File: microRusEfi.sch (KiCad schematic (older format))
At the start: 13 parts, among them U3 Molex_48_pin

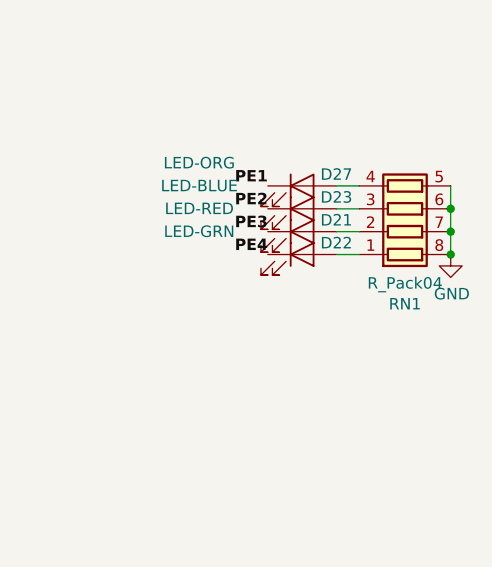
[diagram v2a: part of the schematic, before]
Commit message: Several U# were changed to RN# as they are resistor networks, not semiconductor chips. RN1 is now clearly a 1k. Also some U# were changed to CN#. BOM is now completely populated.
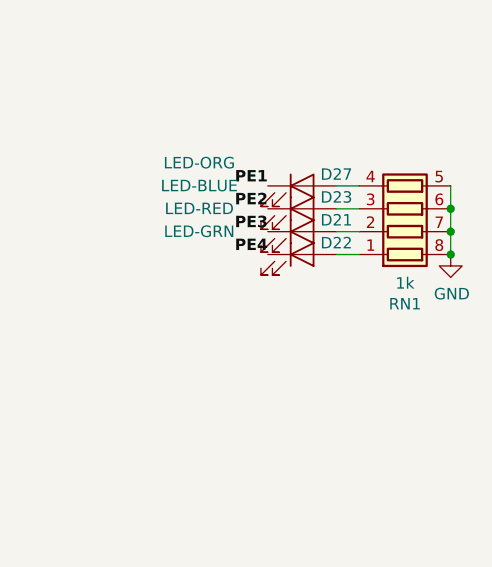
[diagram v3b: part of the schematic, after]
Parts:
- RN1: value R_Pack04 -> 1k; Manufacturer mm -> Panasonic; Part # dd -> EXB-V8V102JV; VEND# vv -> Y4102CT-ND
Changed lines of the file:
@@
 P 15000 5950
 F 0 "RN1" V 14583 5950 50  0000 C CNN
-F 1 "R_Pack04" V 14674 5950 50  0000 C CNN
+F 1 "1k" V 14674 5950 50  0000 C CNN
 F 2 "Resistor_SMD:R_Array_Convex_4x0603" V 15275 5950 50  0001 C CNN
 F 3 "~" H 15000 5950 50  0001 C CNN
-F 4 "dd" H 0   0   50  0001 C CNN "Part #"
+F 4 "EXB-V8V102JV" H 0   0   50  0001 C CNN "Part #"
 F 5 "DIGI" H 0   0   50  0001 C CNN "VEND"
-F 6 "vv" H 0   0   50  0001 C CNN "VEND#"
-F 7 "mm" H 0   0   50  0001 C CNN "Manufacturer"
+F 6 "Y4102CT-ND" H 0   0   50  0001 C CNN "VEND#"
+F 7 "Panasonic " H 0   0   50  0001 C CNN "Manufacturer"
 	1    15000 5950
 	0    1    -1   0

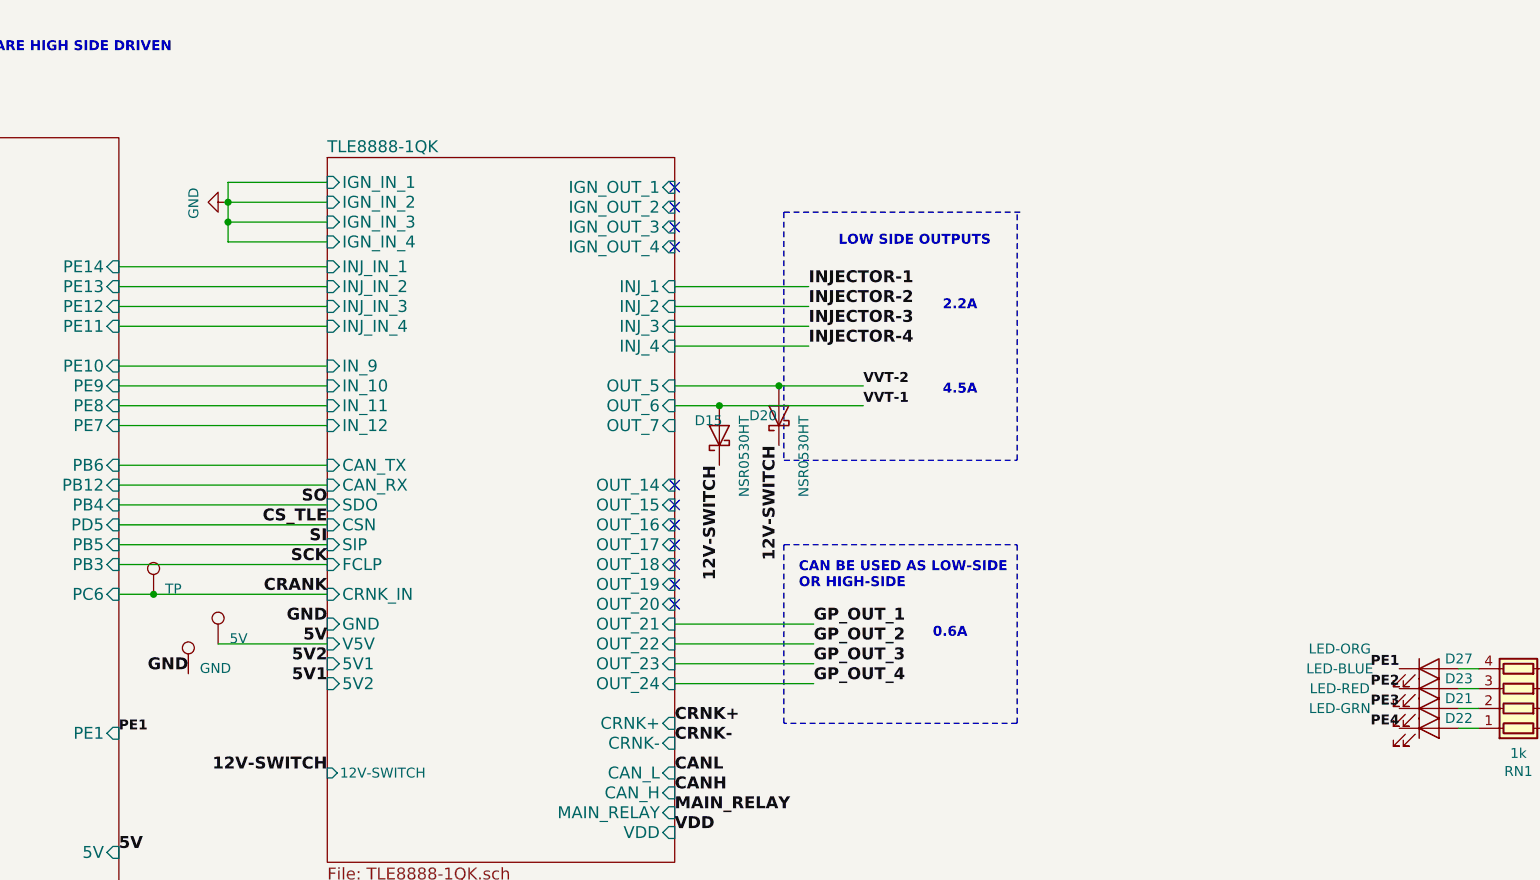
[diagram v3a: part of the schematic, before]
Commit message: Some general MISC cleanup of overlapping text, etc.
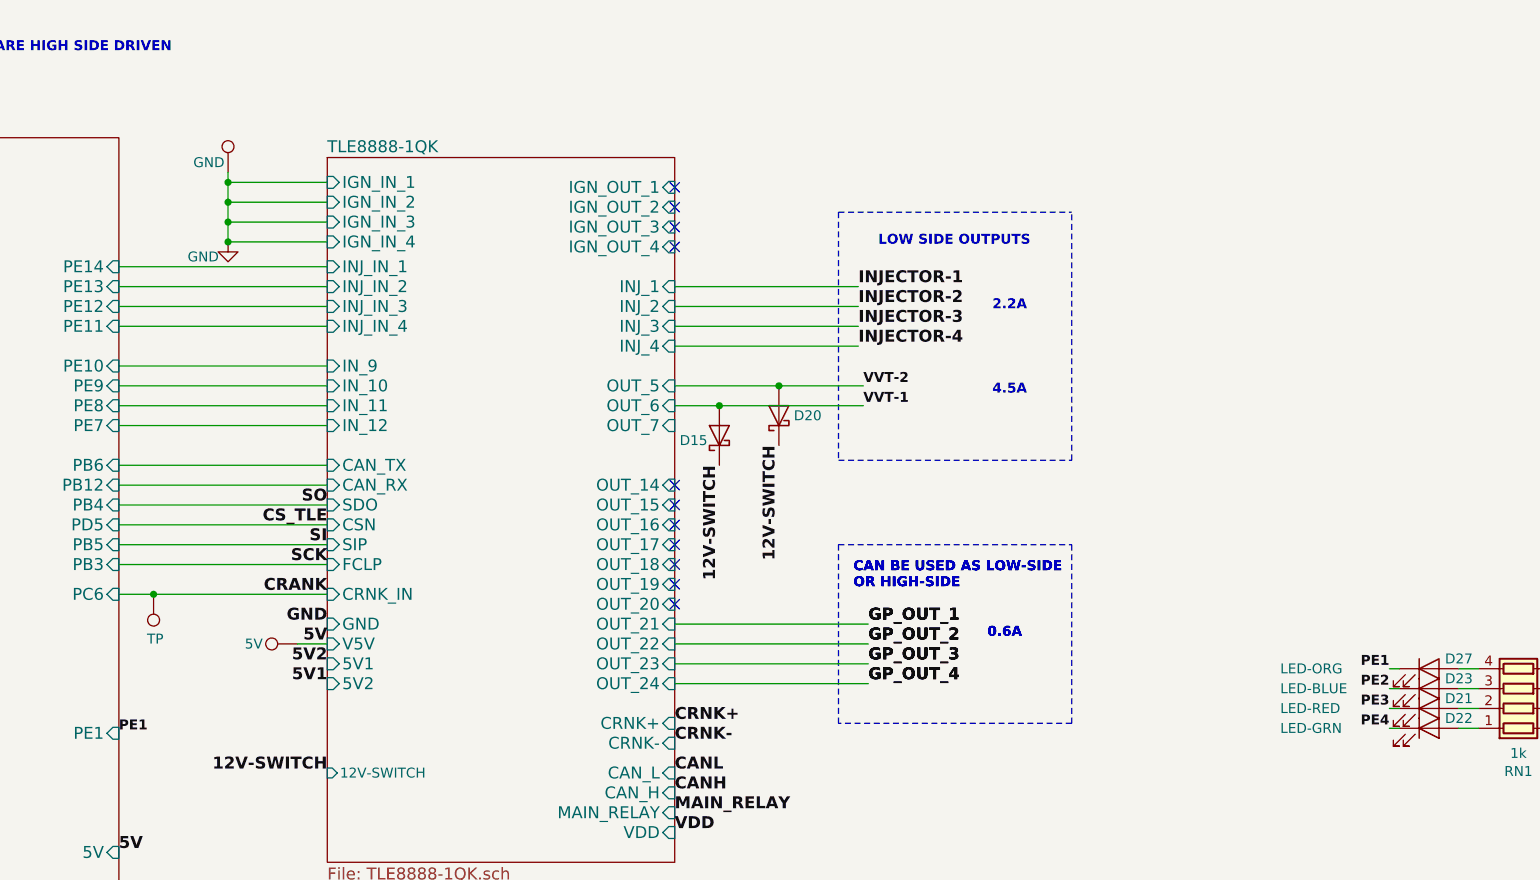
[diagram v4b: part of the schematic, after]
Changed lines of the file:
@@
 Wire Wire Line
 	5600 5075 6700 5075
-Wire Wire Line
-	8450 5725 9000 5725
 Text Label 4050 5225 2    60   ~ 12
 5V
@@
 L Connector:TestPoint TP1
 U 1 1 5C694318
-P 8450 5725
-F 0 "TP1" H 8508 5843 50  0001 L CNN
-F 1 "5V" H 8508 5752 50  0000 L CNN
-F 2 "TestPoint:TestPoint_Pad_D4.0mm" H 8650 5725 50  0001 C CNN
-F 3 "~" H 8650 5725 50  0001 C CNN
-F 4 "DNP" H 0   0   50  0001 C CNN "Part #"
-F 5 "DNP" H 0   0   50  0001 C CNN "VEND"
-F 6 "DNP" H 0   0   50  0001 C CNN "VEND#"
-F 7 "DNP" H 0   0   50  0001 C CNN "Manufacturer"
-	1    8450 5725
-	1    0    0    -1
+P 8850 5725
+F 0 "TP1" H 8908 5843 50  0001 L CNN
+F 1 "5V" V 8850 5900 50  0000 L CNN
+F 2 "TestPoint:TestPoint_Pad_D4.0mm" H 9050 5725 50  0001 C CNN
+F 3 "~" H 9050 5725 50  0001 C CNN
+F 4 "DNP" H 400 0   50  0001 C CNN "Part #"
+F 5 "DNP" H 400 0   50  0001 C CNN "VEND"
+F 6 "DNP" H 400 0   50  0001 C CNN "VEND#"
+F 7 "DNP" H 400 0   50  0001 C CNN "Manufacturer"
+	1    8850 5725
+	0    -1   -1   0
 $EndComp
 Text Label 10750 6675 0    60   ~ 12
@@
 Text Label 9350 8075 0    60   ~ 12
 5V
-Text Label 11450 5925 0    60   ~ 12
+Text Label 11725 5925 0    60   ~ 12
 GP_OUT_4
 Wire Wire Line
@@
 Text Label 9725 7725 0    60   ~ 12
 COIL-4
-Text Label 11425 4025 0    60   ~ 12
+Text Label 11675 4025 0    60   ~ 12
 INJECTOR-2
-Text Label 11425 3925 0    60   ~ 12
+Text Label 11675 3925 0    60   ~ 12
 INJECTOR-1
-Text Label 11425 4125 0    60   ~ 12
+Text Label 11675 4125 0    60   ~ 12
 INJECTOR-3
-Text Label 11425 4225 0    60   ~ 12
+Text Label 11675 4225 0    60   ~ 12
 INJECTOR-4
 $Comp
@@
 U 1 1 5DFFB69F
 P 10975 4675
-F 0 "D15" V 11050 4800 50  0000 R CNN
-F 1 "NSR0530HT" H 11075 4550 50  0000 R CNN
+F 0 "D15" V 10950 4875 50  0000 R CNN
+F 1 "NSR0530HT" H 11075 4550 50  0001 R CNN
 F 2 "Diode_SMD:D_SOD-323" H 10975 4675 50  0001 C CNN
 F 3 "~" H 10975 4675 50  0001 C CNN
@@
 U 1 1 5DFFDCBF
 P 11275 4575
-F 0 "D20" V 11275 4725 50  0000 R CNN
-F 1 "NSR0530HT" H 11275 4450 50  0000 R CNN
+F 0 "D20" V 11275 4500 50  0000 R CNN
+F 1 "NSR0530HT" H 11275 4450 50  0001 R CNN
 F 2 "Diode_SMD:D_SOD-323" H 11275 4575 50  0001 C CNN
 F 3 "~" H 11275 4575 50  0001 C CNN
@@
 Connection ~ 5800 6600
 Wire Wire Line
-	10750 4225 11425 4225
-Wire Wire Line
-	10750 4125 11425 4125
-Wire Wire Line
-	10750 4025 11425 4025
-Wire Wire Line
-	10750 3925 11425 3925
-Text Label 11450 5725 0    60   ~ 12
+	10750 4225 11675 4225
+Wire Wire Line
+	10750 4125 11675 4125
+Wire Wire Line
+	10750 4025 11675 4025
+Wire Wire Line
+	10750 3925 11675 3925
+Text Label 11725 5725 0    60   ~ 12
 GP_OUT_2
-Text Label 11450 5625 0    60   ~ 12
+Text Label 11725 5625 0    60   ~ 12
 GP_OUT_1
-Text Label 11450 5825 0    60   ~ 12
+Text Label 11725 5825 0    60   ~ 12
 GP_OUT_3
-Text Notes 11575 3725 0    50   ~ 10
+Text Notes 11775 3725 0    50   ~ 10
 LOW SIDE OUTPUTS\n
-Text Notes 12100 4475 0    50   ~ 10
+Text Notes 12350 4475 0    50   ~ 10
 4.5A
-Text Notes 12050 5700 0    50   ~ 10
+Text Notes 12325 5700 0    50   ~ 10
 0.6A
 Wire Wire Line
-	10750 5625 11450 5625
-Wire Wire Line
-	10750 5725 11450 5725
-Wire Wire Line
-	10750 5825 11450 5825
-Text Notes 12100 4050 0    50   ~ 10
+	10750 5625 11725 5625
+Wire Wire Line
+	10750 5725 11725 5725
+Wire Wire Line
+	10750 5825 11725 5825
+Text Notes 12350 4050 0    50   ~ 10
 2.2A
 Wire Wire Line
@@
 ANALOG INPUTS.\nADC 1-4 HAS BIAS RESISTORS \nFOR TEMP SENSORS\n\nCAN ALSO BE USED \nAS DIGITAL INPUTS
 Wire Notes Line
-	11300 3550 12500 3550
+	11575 3550 12750 3550
 $Comp
 L Connector:TestPoint TP2
 U 1 1 5D356EBD
-P 8300 5875
-F 0 "TP2" H 8358 5993 50  0001 L CNN
-F 1 "GND" H 8358 5902 50  0000 L CNN
-F 2 "TestPoint:TestPoint_Pad_D4.0mm" H 8500 5875 50  0001 C CNN
-F 3 "~" H 8500 5875 50  0001 C CNN
-F 4 "DNP" H 0   0   50  0001 C CNN "Part #"
-F 5 "DNP" H 0   0   50  0001 C CNN "Manufacturer"
-F 6 "DNP" H 0   0   50  0001 C CNN "VEND"
-F 7 "DNP" H 0   0   50  0001 C CNN "VEND#"
-	1    8300 5875
+P 8500 3350
+F 0 "TP2" H 8558 3468 50  0001 L CNN
+F 1 "GND" H 8325 3400 50  0000 L CNN
+F 2 "TestPoint:TestPoint_Pad_D4.0mm" H 8700 3350 50  0001 C CNN
+F 3 "~" H 8700 3350 50  0001 C CNN
+F 4 "DNP" H 200 -2525 50  0001 C CNN "Part #"
+F 5 "DNP" H 200 -2525 50  0001 C CNN "Manufacturer"
+F 6 "DNP" H 200 -2525 50  0001 C CNN "VEND"
+F 7 "DNP" H 200 -2525 50  0001 C CNN "VEND#"
+	1    8500 3350
 	1    0    0    -1
 $EndComp
-Text Label 8300 5875 2    60   ~ 12
-GND
 Text Label 6000 1575 3    50   ~ 10
 GP_OUT_6
@@
 CAM_SENSOR
 Wire Wire Line
-	10750 5925 11450 5925
+	10750 5925 11725 5925
 Text Label 6100 1575 3    50   ~ 10
 GP_OUT_5
@@
 GP_OUT_5
 Wire Notes Line
-	11300 3550 11300 4800
-Wire Notes Line
-	11300 4800 12475 4800
-Wire Notes Line
-	12475 4800 12475 3550
-Wire Notes Line
-	11300 5225 12475 5225
-Text Notes 11375 5450 0    50   ~ 10
+	11575 3550 11575 4800
+Wire Notes Line
+	11575 4800 12750 4800
+Wire Notes Line
+	12750 4800 12750 3550
+Wire Notes Line
+	11575 5225 12750 5225
+Text Notes 11650 5450 0    50   ~ 10
 CAN BE USED AS LOW-SIDE \nOR HIGH-SIDE
 Wire Notes Line
-	12475 6125 11300 6125
-Wire Notes Line
-	11300 5225 11300 6125
-Wire Notes Line
-	12475 5225 12475 6125
+	12750 6125 11575 6125
+Wire Notes Line
+	11575 5225 11575 6125
+Wire Notes Line
+	12750 5225 12750 6125
 Text Label 4050 5100 2    60   ~ 12
 12V-SWITCH
@@
 Text Label 6700 8525 2    50   ~ 10
 PE4
-Text Label 14400 5850 2    50   ~ 10
+Text Label 14350 5850 2    50   ~ 10
 PE1
 $Comp
@@
 P 14550 6150
 F 0 "D22" H 14700 6200 50  0000 C CNN
-F 1 "LED-GRN" H 14100 6250 50  0000 C CNN
+F 1 "LED-GRN" H 13800 6150 50  0000 L CNN
 F 2 "LED_SMD:LED_0603_1608Metric" H 14550 6150 50  0001 C CNN
 F 3 "~" H 14550 6150 50  0001 C CNN
@@
 P 8125 5475
 F 0 "TP4" H 8183 5593 50  0001 L CNN
-F 1 "TP" H 8183 5502 50  0000 L CNN
+F 1 "TP" H 8075 5700 50  0000 L CNN
 F 2 "TestPoint:TestPoint_Pad_D2.0mm" H 8325 5475 50  0001 C CNN
 F 3 "~" H 8325 5475 50  0001 C CNN
@@
 F 7 "DNP" H 0   0   50  0001 C CNN "Manufacturer"
 	1    8125 5475
-	1    0    0    -1
+	-1   0    0    1
 $EndComp
 Connection ~ 8125 5475
@@
 L power:GND #PWR0183
 U 1 1 5D16B569
-P 8500 3500
-F 0 "#PWR0183" H 8500 3250 50  0001 C CNN
-F 1 "GND" H 8505 3327 50  0000 C CNN
-F 2 "" H 8500 3500 50  0001 C CNN
-F 3 "" H 8500 3500 50  0001 C CNN
-	1    8500 3500
-	0    1    1    0
+P 8500 3700
+F 0 "#PWR0183" H 8500 3450 50  0001 C CNN
+F 1 "GND" H 8375 3625 50  0000 C CNN
+F 2 "" H 8500 3700 50  0001 C CNN
+F 3 "" H 8500 3700 50  0001 C CNN
+	1    8500 3700
+	1    0    0    -1
 $EndComp
 Wire Wire Line
@@
 P 14550 6050
 F 0 "D21" H 14700 6100 50  0000 C CNN
-F 1 "LED-RED" H 14100 6150 50  0000 C CNN
+F 1 "LED-RED" H 13800 6050 50  0000 L CNN
 F 2 "LED_SMD:LED_0603_1608Metric" H 14550 6050 50  0001 C CNN
 F 3 "~" H 14550 6050 50  0001 C CNN
@@
 P 14550 5950
 F 0 "D23" H 14700 6000 50  0000 C CNN
-F 1 "LED-BLUE" H 14100 6050 50  0000 C CNN
+F 1 "LED-BLUE" H 13800 5950 50  0000 L CNN
 F 2 "LED_SMD:LED_0603_1608Metric" H 14550 5950 50  0001 C CNN
 F 3 "~" H 14550 5950 50  0001 C CNN
@@
 P 14550 5850
 F 0 "D27" H 14700 5900 50  0000 C CNN
-F 1 "LED-ORG" H 14100 5950 50  0000 C CNN
+F 1 "LED-ORG" H 13800 5850 50  0000 L CNN
 F 2 "LED_SMD:LED_0603_1608Metric" H 14550 5850 50  0001 C CNN
 F 3 "~" H 14550 5850 50  0001 C CNN
@@
 	1    0    0    -1
 $EndComp
-Text Label 14400 5950 2    50   ~ 10
+Text Label 14350 5950 2    50   ~ 10
 PE2
-Text Label 14400 6050 2    50   ~ 10
+Text Label 14350 6050 2    50   ~ 10
 PE3
-Text Label 14400 6150 2    50   ~ 10
+Text Label 14350 6150 2    50   ~ 10
 PE4
 $Comp
@@
 Wire Wire Line
 	14700 6150 14800 6150
+Connection ~ 8500 3400
+Wire Wire Line
+	8500 3350 8500 3400
+Connection ~ 8500 3700
+Wire Wire Line
+	8850 5725 9000 5725
+Text Label 11725 5925 0    60   ~ 12
+GP_OUT_4
+Text Label 11725 5725 0    60   ~ 12
+GP_OUT_2
+Text Label 11725 5625 0    60   ~ 12
+GP_OUT_1
+Text Label 11725 5825 0    60   ~ 12
+GP_OUT_3
+Text Notes 12325 5700 0    50   ~ 10
+0.6A
+Text Notes 11650 5450 0    50   ~ 10
+CAN BE USED AS LOW-SIDE \nOR HIGH-SIDE
+Wire Wire Line
+	14350 5850 14400 5850
+Wire Wire Line
+	14350 5950 14400 5950
+Wire Wire Line
+	14350 6050 14400 6050
+Wire Wire Line
+	14350 6150 14400 6150
 $EndSCHEMATC
